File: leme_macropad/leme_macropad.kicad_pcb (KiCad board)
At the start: 4 copper layers, 99.9 x 63.9 mm, 93 parts, among them J1 USB_C_Receptacle_USB2.0_16P, J2 OLED display, SW1 SW_Push, SW10 SW_Push, SW2 SW_Push, SW3 SW_Push, SW4 SW_Push, SW5 SW_Push, SW6 SW_Push, SW7 RotaryEncoder_Switch, SW9 SW_Push, U1 SRV05-4HTG-D, U2 NCP1117-3.3_SOT223, U3 W25Q128JVS, U4 RP2040, Y1 ABM8-272-T3

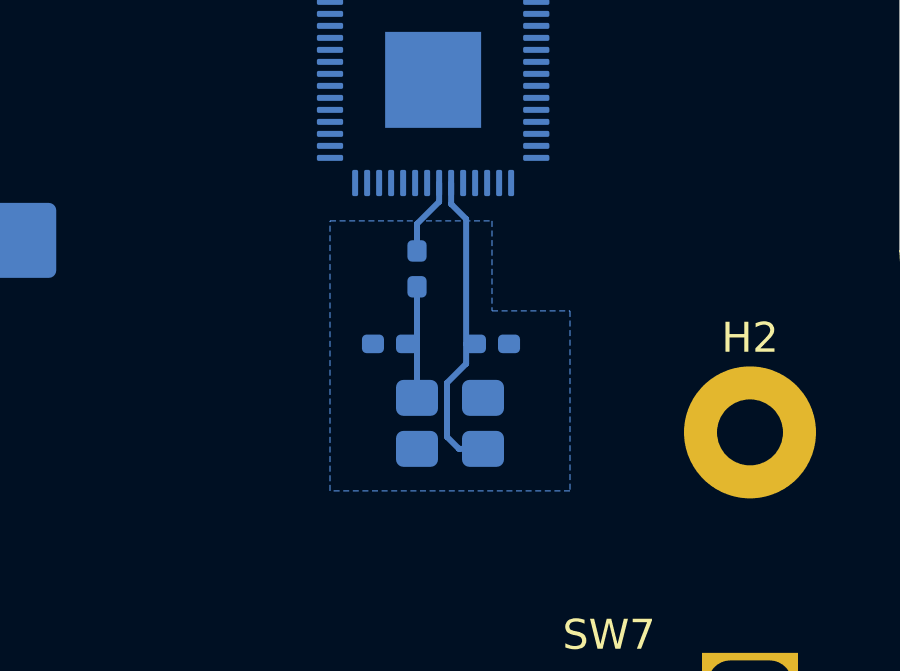
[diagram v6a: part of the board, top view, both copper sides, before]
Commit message: Reorganizes crystal oscillator after changing passives to 0402
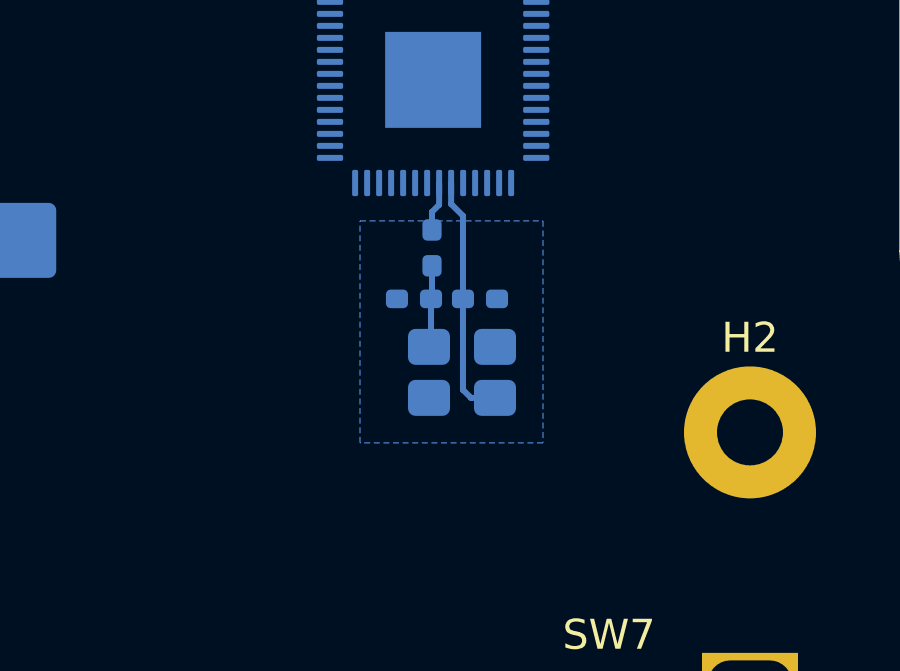
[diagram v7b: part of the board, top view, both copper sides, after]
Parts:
- moved Y1 1.75 mm to (180.4, 94.0)
- moved C7 1.70 mm to (178.8, 91.6)
- moved C6 1.55 mm to (181.0, 91.6)
- moved R3 0.86 mm to (179.4, 89.9)
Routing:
- net XIN: track 10.3 -> 8.24 mm
- net Net-(C7-Pad2): track 3.42 -> 2.74 mm
- net XOUT: track 2.26 -> 1.66 mm
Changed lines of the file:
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@@
 	(footprint "Capacitor_SMD:C_0402_1005Metric_Pad0.74x0.62mm_HandSolder"
 		(layer "B.Cu")
-		(at 181.4 93.1 180)
+		(at 181 91.6 180)
 		(descr "Capacitor SMD 0402 (1005 Metric), square (rectangular) end terminal, IPC-7351 nominal with elongated pad for handsoldering. (Body size source: IPC-SM-782 page 76, https://www.pcb-3d.com/wordpress/wp-content/uploads/ipc-sm-782a_amendment_1_and_2.pdf), generated with kicad-footprint-generator")
 		(tags "capacitor handsolder")
@@
 	(footprint "Resistor_SMD:R_0402_1005Metric_Pad0.72x0.64mm_HandSolder"
 		(layer "B.Cu")
-		(at 178.9 90.6 90)
+		(at 179.4 89.9 90)
 		(descr "Resistor SMD 0402 (1005 Metric), square (rectangular) end terminal, IPC-7351 nominal with elongated pad for handsoldering. (Body size source: IPC-SM-782 page 72, https://www.pcb-3d.com/wordpress/wp-content/uploads/ipc-sm-782a_amendment_1_and_2.pdf), generated with kicad-footprint-generator")
 		(tags "resistor handsolder")
@@
 	(footprint "Crystal:Crystal_SMD_3225-4Pin_3.2x2.5mm"
 		(layer "B.Cu")
-		(at 180 95.75 180)
+		(at 180.4 94.05 180)
 		(descr "SMD3225/4, Crystal, 3.2x2.5mm package, SMD, generated with kicad-footprint-generator make_crystal.py, http://www.txccrystal.com/images/pdf/7m-accuracy.pdf")
 		(property "Reference" "Y1"
@@
 	(footprint "Capacitor_SMD:C_0402_1005Metric_Pad0.74x0.62mm_HandSolder"
 		(layer "B.Cu")
-		(at 178 93.1)
+		(at 178.8 91.6)
 		(descr "Capacitor SMD 0402 (1005 Metric), square (rectangular) end terminal, IPC-7351 nominal with elongated pad for handsoldering. (Body size source: IPC-SM-782 page 76, https://www.pcb-3d.com/wordpress/wp-content/uploads/ipc-sm-782a_amendment_1_and_2.pdf), generated with kicad-footprint-generator")
 		(tags "capacitor handsolder")
@@
 	)
 	(segment
-		(start 180.0375 87.7375)
-		(end 180.0375 88.4375)
-		(width 0.2)
-		(layer "B.Cu")
-		(net 4)
-	)
-	(segment
-		(start 180.5375 88.9375)
-		(end 180.5375 93.1)
-		(width 0.2)
-		(layer "B.Cu")
-		(net 4)
-	)
-	(segment
-		(start 179.9 96.2)
-		(end 180.3 96.6)
+		(start 180.7 94.9)
+		(end 181.5 94.9)
 		(width 0.2)
 		(layer "B.Cu")
@@
 	)
 	(segment
-		(start 180.0375 88.4375)
-		(end 180.5375 88.9375)
+		(start 180.4325 91.6)
+		(end 180.4325 94.6325)
 		(width 0.2)
 		(layer "B.Cu")
@@
 	)
 	(segment
-		(start 180.5375 93.7625)
-		(end 179.9 94.4)
+		(start 180.0375 87.7375)
+		(end 180.0375 88.4375)
 		(width 0.2)
 		(layer "B.Cu")
@@
 	)
 	(segment
-		(start 180.3 96.6)
-		(end 181.1 96.6)
+		(start 180.4325 94.6325)
+		(end 180.7 94.9)
 		(width 0.2)
 		(layer "B.Cu")
@@
 	)
 	(segment
-		(start 180.5375 93.1)
-		(end 180.5375 93.7625)
+		(start 180.4325 88.8325)
+		(end 180.4325 91.6)
 		(width 0.2)
 		(layer "B.Cu")
@@
 	)
 	(segment
-		(start 179.9 94.4)
-		(end 179.9 96.2)
+		(start 180.0375 88.4375)
+		(end 180.4325 88.8325)
 		(width 0.2)
 		(layer "B.Cu")
@@
 	)
 	(segment
-		(start 178.9 94.9)
-		(end 178.9 93.1375)
+		(start 179.3675 93.1325)
+		(end 179.3 93.2)
 		(width 0.2)
 		(layer "B.Cu")
@@
 	)
 	(segment
-		(start 178.9 91.5125)
-		(end 178.9 93.0625)
+		(start 179.3675 91.6)
+		(end 179.3675 93.1325)
 		(width 0.2)
 		(layer "B.Cu")
@@
 	)
 	(segment
-		(start 178.9 93.0625)
-		(end 178.8625 93.1)
+		(start 179.4 91.5675)
+		(end 179.3675 91.6)
 		(width 0.2)
 		(layer "B.Cu")
@@
 	)
 	(segment
-		(start 178.9 93.1375)
-		(end 178.8625 93.1)
+		(start 179.4 90.4975)
+		(end 179.4 91.5675)
 		(width 0.2)
 		(layer "B.Cu")
@@
 	)
 	(segment
-		(start 178.9 89.1)
-		(end 179.6375 88.3625)
+		(start 179.6375 87.7375)
+		(end 179.6375 88.4625)
 		(width 0.2)
 		(layer "B.Cu")
@@
 	)
 	(segment
-		(start 179.6375 88.3625)
-		(end 179.6375 87.7375)
+		(start 179.4 88.7)
+		(end 179.4 89.3025)
 		(width 0.2)
 		(layer "B.Cu")
@@
 	)
 	(segment
-		(start 178.9 89.6875)
-		(end 178.9 89.1)
+		(start 179.6375 88.4625)
+		(end 179.4 88.7)
 		(width 0.2)
 		(layer "B.Cu")
@@
 		(polygon
 			(pts
-				(xy 176 89) (xy 181.4 89) (xy 181.4 92) (xy 184 92) (xy 184 98) (xy 176 98)
+				(xy 177 89) (xy 183.1 89) (xy 183.1 96.4) (xy 177 96.4)
 			)
 		)

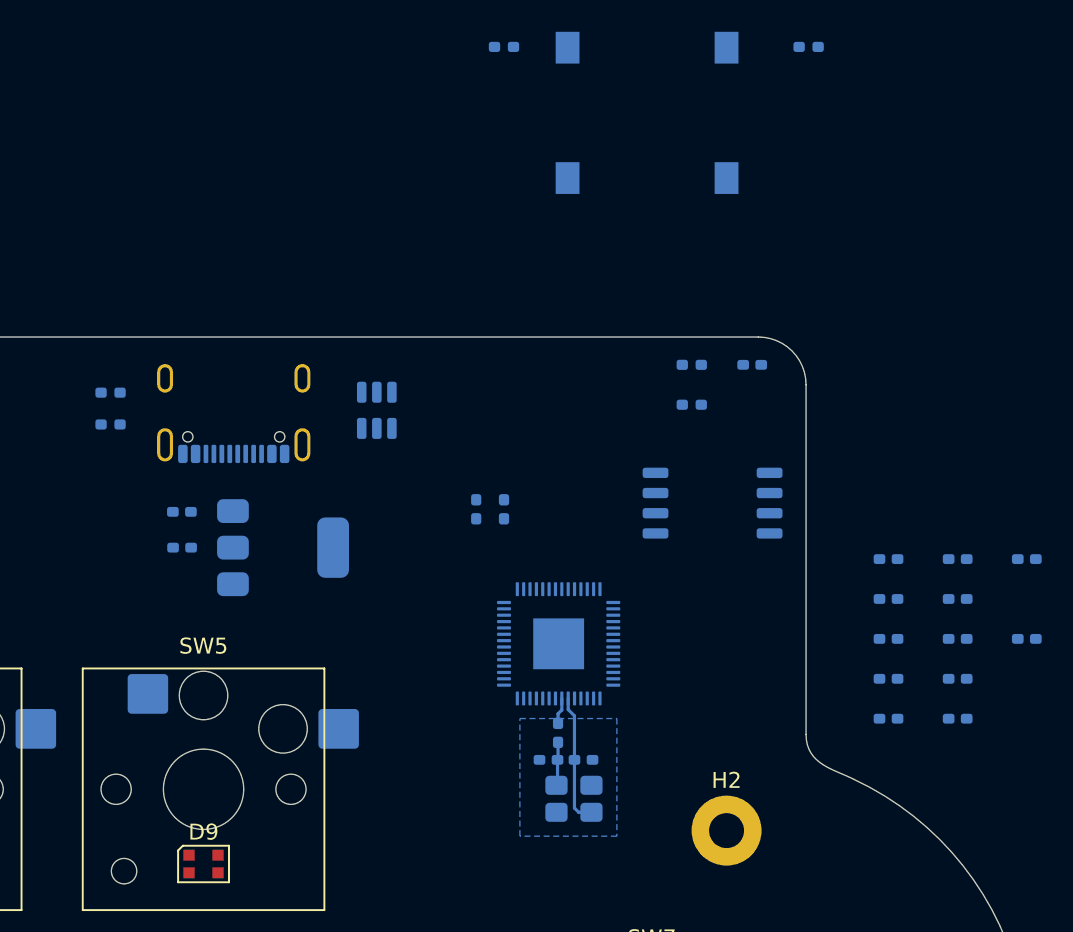
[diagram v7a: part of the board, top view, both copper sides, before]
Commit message: Roughly positions decoupling caps and 3.3v main rail
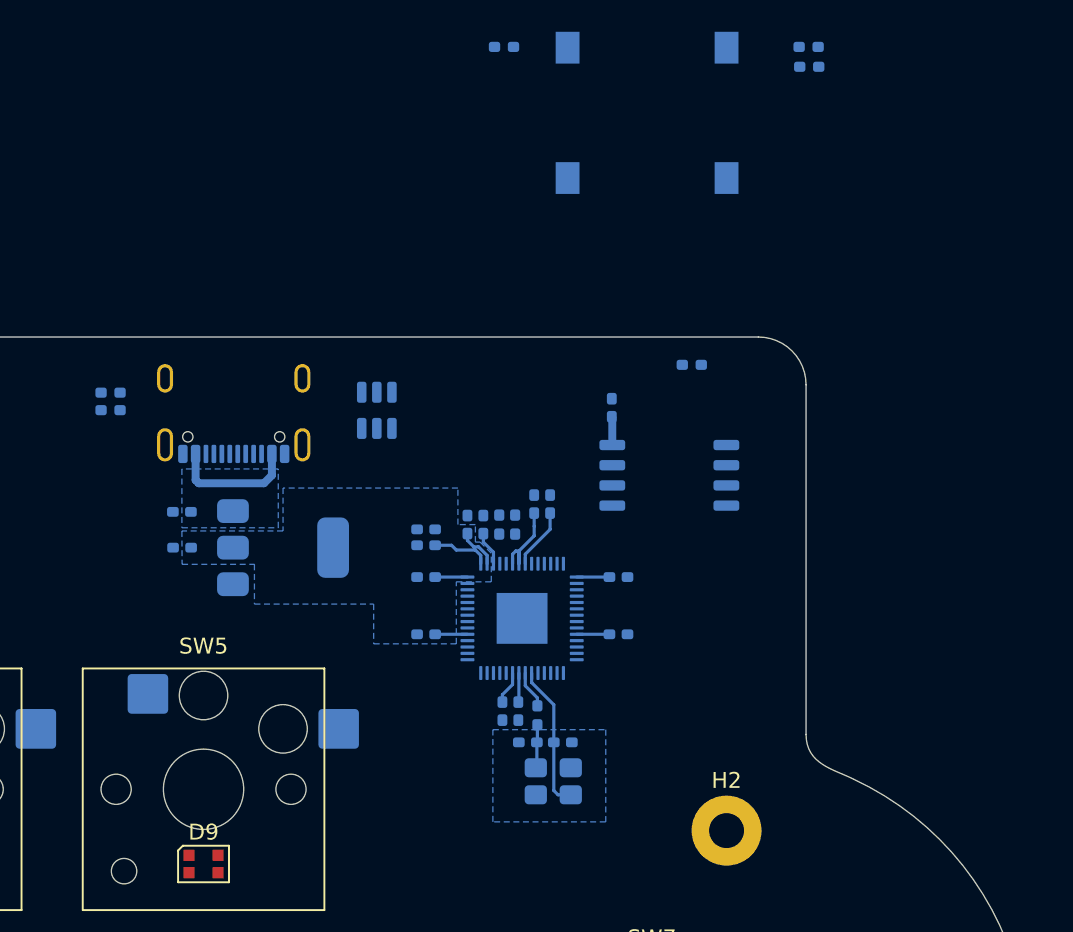
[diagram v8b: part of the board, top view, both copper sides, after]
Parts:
- moved C3 37.8 mm to (171.1, 77.1)
- moved C11 34.0 mm to (171.1, 80.1)
- moved C8 33.4 mm to (171.1, 78.1)
- moved C5 32.1 mm to (177.9, 75.5), turned to 90 degrees
- moved C13 29.5 mm to (171.1, 83.7)
- moved C17 29.2 mm to (173.7, 76.8), turned to 90 degrees
- moved C12 29.0 mm to (178.9, 75.5), turned to 90 degrees
- moved C16 27.3 mm to (174.7, 76.8), turned to 90 degrees
- moved C14 25.3 mm to (175.9, 88.5), turned to -90 degrees
- moved C15 23.7 mm to (176.9, 88.5), turned to -90 degrees
- moved R5 22.5 mm to (195.2, 48.0), turned to 0 degrees
- moved C9 21.4 mm to (183.2, 80.1), turned to 0 degrees
- moved C10 21.3 mm to (183.2, 83.7), turned to 0 degrees
- moved C4 9.24 mm to (182.8, 69.5), turned to 90 degrees
- moved U3 3.23 mm to (186.4, 73.7)
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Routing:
- net +3.3V: track 0.00 -> 23.5 mm
- net +1V1: track 0.00 -> 8.08 mm
- net +5V: track 0.00 -> 8.08 mm
- net XIN: track 8.24 -> 9.15 mm
- net XOUT: track 1.66 -> 2.38 mm
- added copper zone on B.Cu, net +3.3V
- added copper zone on B.Cu, net +5V
